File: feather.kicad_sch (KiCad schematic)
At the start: 1 part

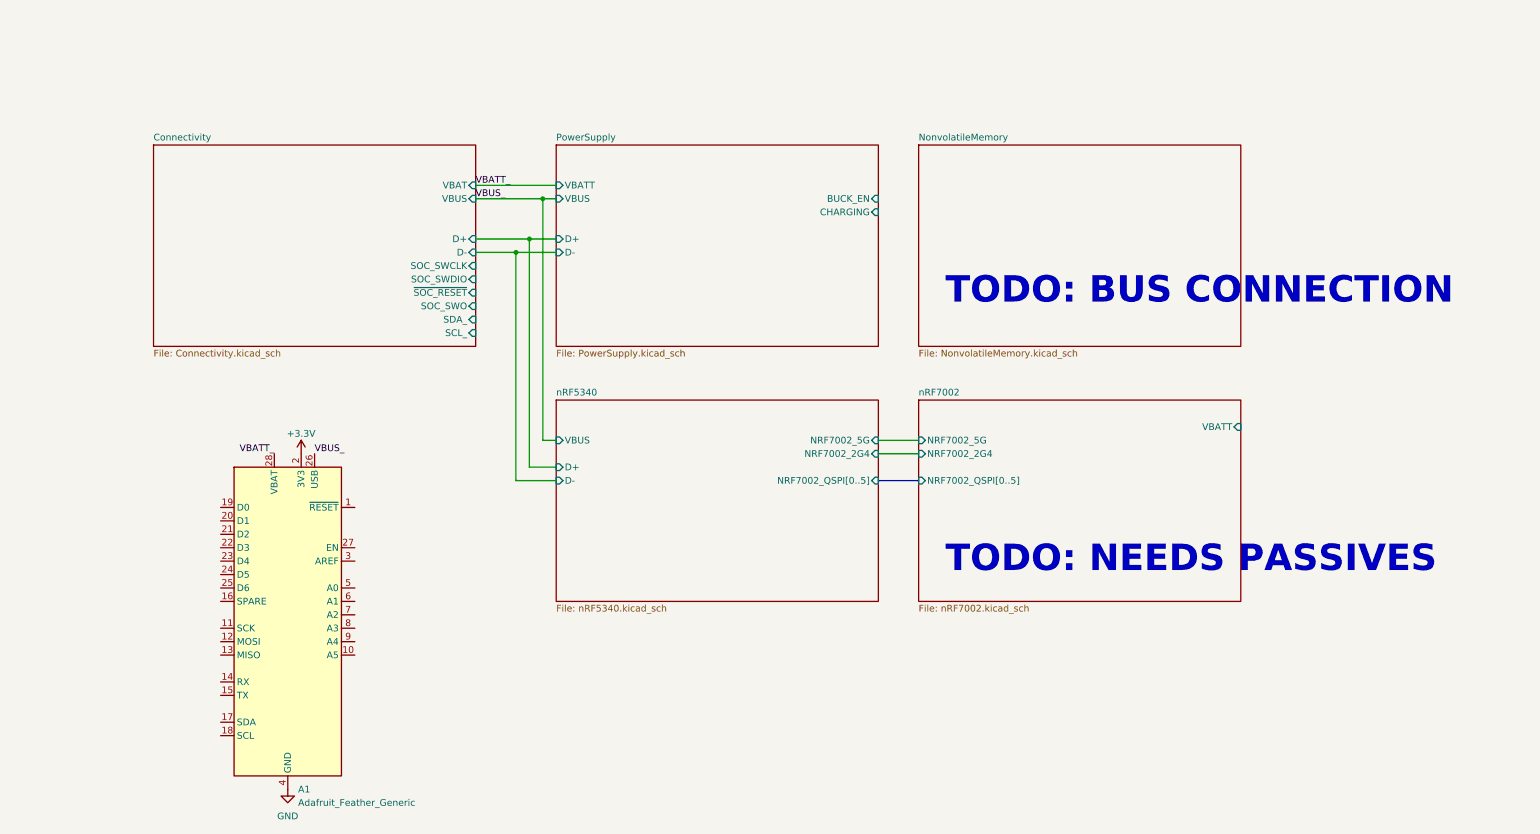
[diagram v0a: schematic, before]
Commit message: Added passvies and bus connections to nRF7002
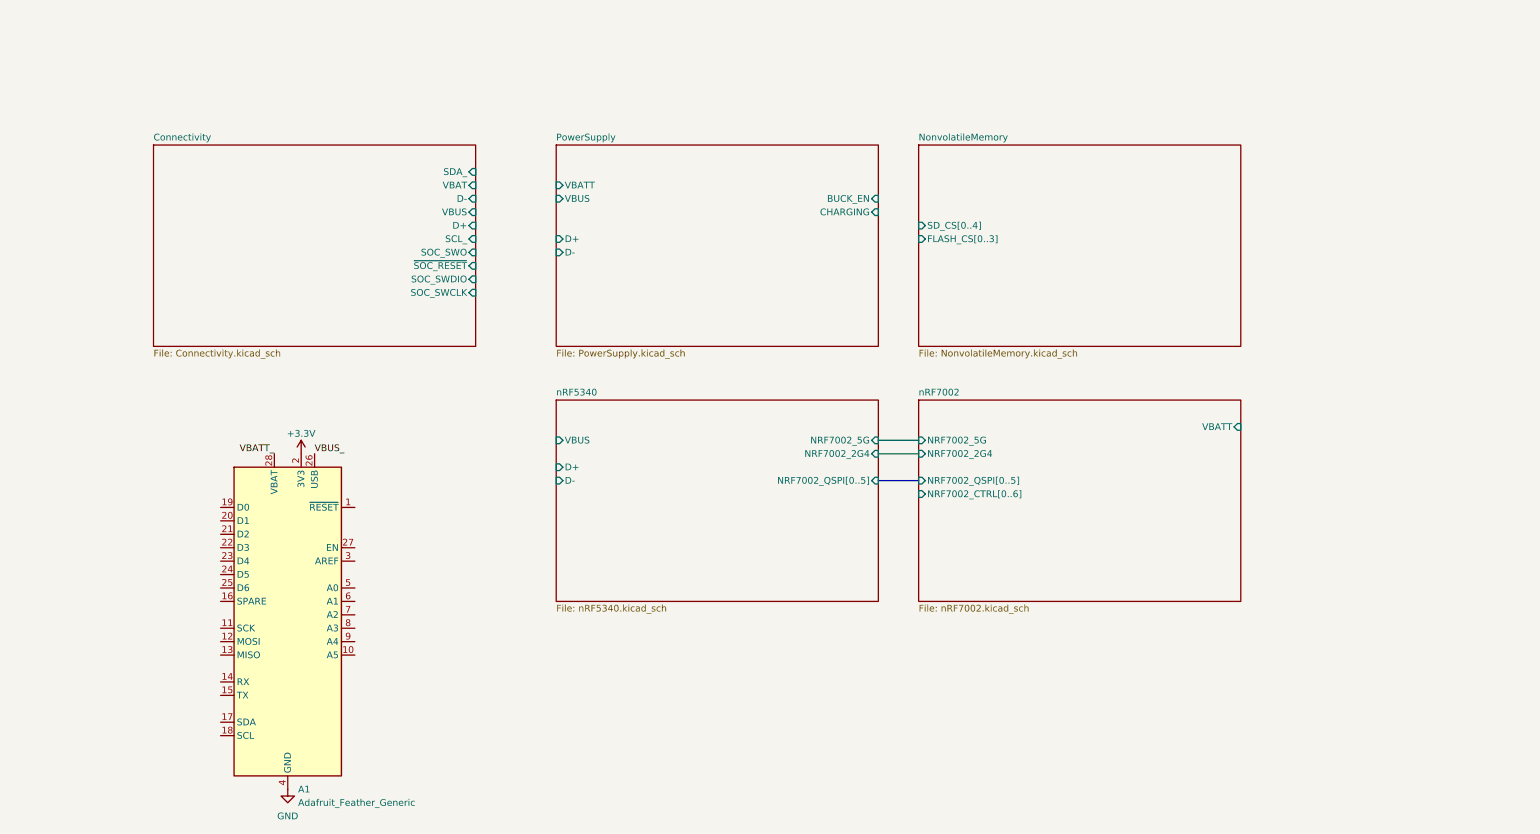
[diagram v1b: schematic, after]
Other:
- sheet NonvolatileMemory ports: added FLASH_CS[0..3], SD_CS[0..4]; removed none
- sheet nRF7002 ports: added NRF7002_CTRL[0..6]; removed none
- note removed: "TODO: BUS CONNECTION"
- note removed: "TODO: NEEDS PASSIVES"
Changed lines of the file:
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@@
 (kicad_sch (version 20230121) (generator eeschema)
   (paper "A4")
-  (junction (at 116.84 55.88) (diameter 0) (color 0 0 0 0)
-  )
-  (junction (at 119.38 48.26) (diameter 0) (color 0 0 0 0)
-  )
-  (junction (at 114.3 58.42) (diameter 0) (color 0 0 0 0)
-  )
-  (wire (pts (xy 106.68 58.42) (xy 114.3 58.42))
-    (stroke (width 0) (type default))
-  )
-  (wire (pts (xy 119.38 93.98) (xy 121.92 93.98))
-    (stroke (width 0) (type default))
-  )
   (wire (pts (xy 182.88 96.52) (xy 190.5 96.52))
     (stroke (width 0) (type default))
   )
-  (wire (pts (xy 106.68 45.72) (xy 121.92 45.72))
-    (stroke (width 0) (type default))
-  )
-  (wire (pts (xy 106.68 55.88) (xy 116.84 55.88))
-    (stroke (width 0) (type default))
-  )
-  (wire (pts (xy 121.92 101.6) (xy 114.3 101.6))
-    (stroke (width 0) (type default))
-  )
   (bus (pts (xy 182.88 101.6) (xy 190.5 101.6))
     (stroke (width 0) (type default))
   )
-  (wire (pts (xy 119.38 48.26) (xy 121.92 48.26))
-    (stroke (width 0) (type default))
-  )
   (wire (pts (xy 182.88 93.98) (xy 190.5 93.98))
     (stroke (width 0) (type default))
   )
-  (wire (pts (xy 121.92 99.06) (xy 116.84 99.06))
-    (stroke (width 0) (type default))
-  )
-  (wire (pts (xy 119.38 48.26) (xy 119.38 93.98))
-    (stroke (width 0) (type default))
-  )
-  (wire (pts (xy 116.84 55.88) (xy 121.92 55.88))
-    (stroke (width 0) (type default))
-  )
-  (wire (pts (xy 114.3 101.6) (xy 114.3 58.42))
-    (stroke (width 0) (type default))
-  )
-  (wire (pts (xy 116.84 99.06) (xy 116.84 55.88))
-    (stroke (width 0) (type default))
-  )
-  (wire (pts (xy 114.3 58.42) (xy 121.92 58.42))
-    (stroke (width 0) (type default))
-  )
-  (wire (pts (xy 106.68 48.26) (xy 119.38 48.26))
-    (stroke (width 0) (type default))
-  )
-  (text "TODO: BUS CONNECTION" (at 195.58 68.58 0)
-    (effects (font (size 5 5) (thickness 2) bold) (justify left bottom))
-  )
-  (text "TODO: NEEDS PASSIVES" (at 195.58 119.38 0)
-    (effects (font (size 5 5) (thickness 2) bold) (justify left bottom))
-  )
   (label "VBUS_" (at 76.2 96.52 0) (fields_autoplaced)
     (effects (font (size 1.27 1.27)) (justify left bottom))
@@
   (label "VBATT_" (at 68.58 96.52 180) (fields_autoplaced)
     (effects (font (size 1.27 1.27)) (justify right bottom))
-  )
-  (label "VBUS_" (at 106.68 48.26 0) (fields_autoplaced)
-    (effects (font (size 1.27 1.27)) (justify left bottom))
-  )
-  (label "VBATT_" (at 106.68 45.72 0) (fields_autoplaced)
-    (effects (font (size 1.27 1.27)) (justify left bottom))
   )
   (symbol (lib_id "power:+3.3V") (at 73.66 96.52 0) (unit 1)
@@
       (effects (font (size 1.27 1.27)) (justify left top))
     )
+    (pin "FLASH_CS[0..3]" input (at 190.5 55.88 180)
+      (effects (font (size 1.27 1.27)) (justify left))
+    )
+    (pin "SD_CS[0..4]" input (at 190.5 53.34 180)
+      (effects (font (size 1.27 1.27)) (justify left))
+    )
     (instances
       (project "feather"
@@
       (effects (font (size 1.27 1.27)) (justify left top))
     )
-    (pin "SOC_SWO" input (at 106.68 68.58 0)
-      (effects (font (size 1.27 1.27)) (justify right))
-    )
-    (pin "~{SOC_RESET}" input (at 106.68 66.04 0)
+    (pin "SDA_" input (at 106.68 43.18 0)
+      (effects (font (size 1.27 1.27)) (justify right))
+    )
+    (pin "VBAT" input (at 106.68 45.72 0)
+      (effects (font (size 1.27 1.27)) (justify right))
+    )
+    (pin "D-" input (at 106.68 48.26 0)
+      (effects (font (size 1.27 1.27)) (justify right))
+    )
+    (pin "VBUS" input (at 106.68 50.8 0)
+      (effects (font (size 1.27 1.27)) (justify right))
+    )
+    (pin "D+" input (at 106.68 53.34 0)
+      (effects (font (size 1.27 1.27)) (justify right))
+    )
+    (pin "SCL_" input (at 106.68 55.88 0)
+      (effects (font (size 1.27 1.27)) (justify right))
+    )
+    (pin "SOC_SWO" input (at 106.68 58.42 0)
+      (effects (font (size 1.27 1.27)) (justify right))
+    )
+    (pin "~{SOC_RESET}" input (at 106.68 60.96 0)
       (effects (font (size 1.27 1.27)) (justify right))
     )
@@
       (effects (font (size 1.27 1.27)) (justify right))
     )
-    (pin "SOC_SWCLK" input (at 106.68 60.96 0)
-      (effects (font (size 1.27 1.27)) (justify right))
-    )
-    (pin "D-" input (at 106.68 58.42 0)
-      (effects (font (size 1.27 1.27)) (justify right))
-    )
-    (pin "D+" input (at 106.68 55.88 0)
-      (effects (font (size 1.27 1.27)) (justify right))
-    )
-    (pin "VBAT" input (at 106.68 45.72 0)
-      (effects (font (size 1.27 1.27)) (justify right))
-    )
-    (pin "SCL_" input (at 106.68 73.66 0)
-      (effects (font (size 1.27 1.27)) (justify right))
-    )
-    (pin "SDA_" input (at 106.68 71.12 0)
-      (effects (font (size 1.27 1.27)) (justify right))
-    )
-    (pin "VBUS" input (at 106.68 48.26 0)
+    (pin "SOC_SWCLK" input (at 106.68 66.04 0)
       (effects (font (size 1.27 1.27)) (justify right))
     )
@@
       (effects (font (size 1.27 1.27)) (justify left))
     )
+    (pin "NRF7002_CTRL[0..6]" input (at 190.5 104.14 180)
+      (effects (font (size 1.27 1.27)) (justify left))
+    )

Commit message: Schematic complete.
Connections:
- net ~{RESET}: now reaches A1.1 (~{RESET})
- net AIN5: now reaches A1.10 (A5)
- net OUT_SPI0: now reaches A1.11 (SCK)
- net OUT_SPI1: now reaches A1.12 (MOSI)
- net OUT_SPI2: now reaches A1.13 (MISO)
- net OUT_UART0: now reaches A1.14 (RX)
- net OUT_UART1: now reaches A1.15 (TX)
- net OUT7: now reaches A1.16 (SPARE)
- net OUT_TWI0: now reaches A1.17 (SDA)
- net OUT_TWI1: now reaches A1.18 (SCL)
- net OUT0: now reaches A1.19 (D0)
- net OUT1: now reaches A1.20 (D1)
- net OUT2: now reaches A1.21 (D2)
- net OUT3: now reaches A1.22 (D3)
- net OUT4: now reaches A1.23 (D4)
- net OUT5: now reaches A1.24 (D5)
- net OUT6: now reaches A1.25 (D6)
- net REG_EN: now reaches A1.27 (EN)
- net AIN0: now reaches A1.5 (A0)
- net AIN1: now reaches A1.6 (A1)
- net AIN2: now reaches A1.7 (A2)
- net AIN3: now reaches A1.8 (A3)
- net AIN4: now reaches A1.9 (A4)
- net +3.3V renamed +3V3
- no-connect marks 0 -> 1
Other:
- sheet Connectivity ports: added CC1, CC2, STEMMA_SCL, STEMMA_SDA; removed SCL_, SDA_, SOC_SWO
- sheet NonvolatileMemory ports: added FLASH_SD_CTRL[0..4], FLASH_VDD_IN, SD_CARD_EN, SD_INSERTED; removed FLASH_CS[0..3], SD_CS[0..4]
- sheet PowerSupply ports: added CC1, CC2, LSIN1, LSIN2, LSOUT1, LSOUT2, NPM_SCL, NPM_SDA, REG_EN, VBAT, VBUS_IN, VBUS_OUT, VSYS; removed BUCK_EN, CHARGING, D+, D-, VBATT, VBUS
- sheet nRF5340 ports: added AIN[0..5], FLASH_SD_CTRL[0..4], NRF7002_CTRL[0..6], OUT[0..7], OUT_SPI[0..2], OUT_TWI[0..1], OUT_UART[0..1], SCL, SDA, SD_ENABLE, SD_INSERTED, SWDCLK, SWDIO, ~{RESET}; removed none
- sheet nRF7002 ports: added IOVDD_IN; removed VBATT
- moved on the sheet: A1
